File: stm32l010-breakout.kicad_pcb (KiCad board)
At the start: 2 copper layers, 24 x 50 mm, 30 parts, among them J1 SWD, J2 Left, J3 Right, Q1 BC847CDW1, SW1 Reset, U1 STM32L010K8Tx, Y1 32.768kHz

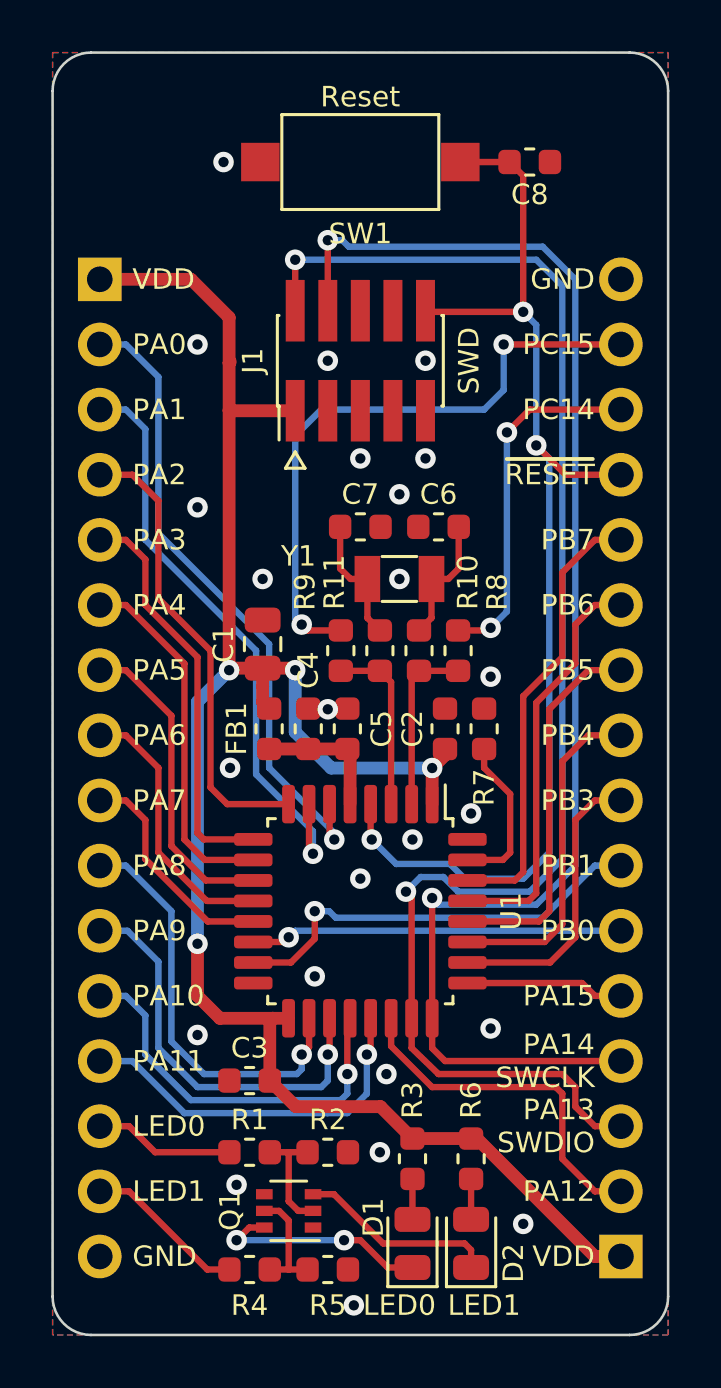
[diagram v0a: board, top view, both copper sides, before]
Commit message: Rotated the SWD connector, moved LED buffer to the front layer
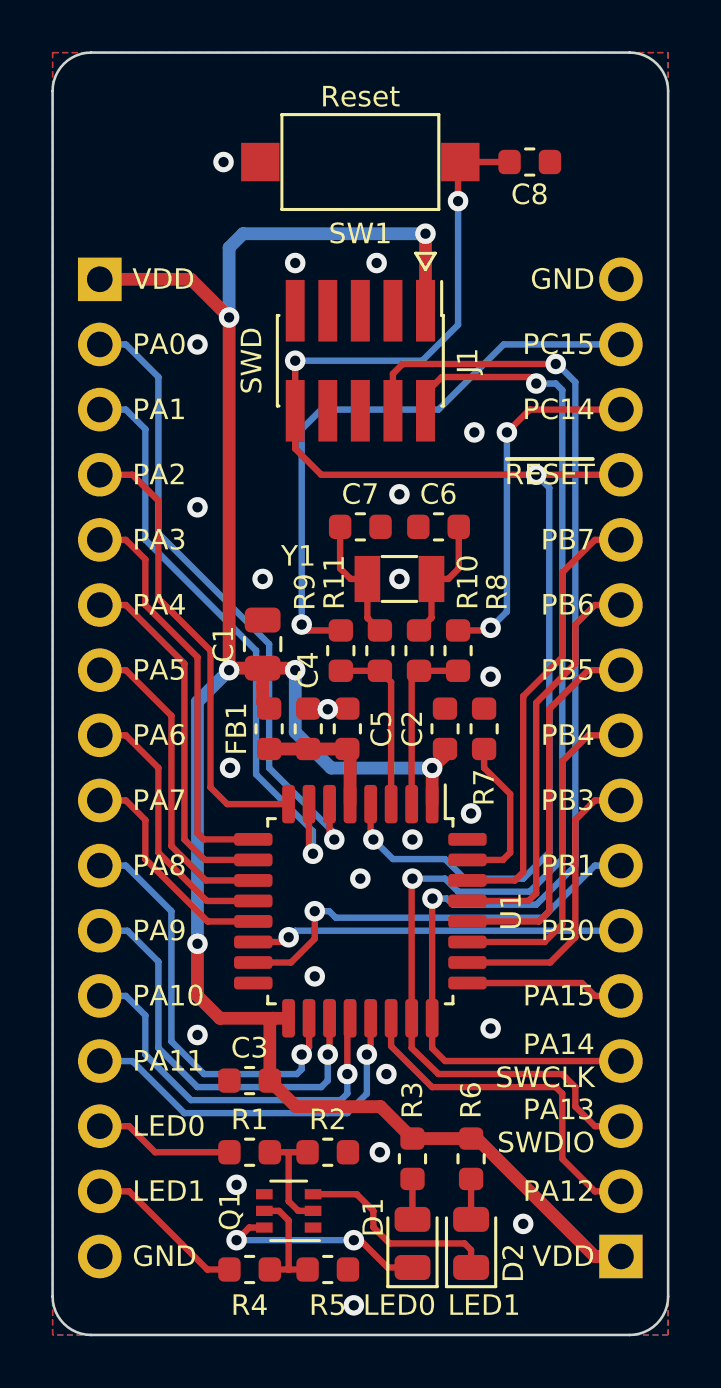
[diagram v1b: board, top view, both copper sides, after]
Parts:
- turned J1 to 270 degrees
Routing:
- net VDD: track 73.2 -> 84.2 mm, vias 4 -> 6
- net /PA13_SWDIO: track 58.3 -> 47.8 mm
- net /~RESET: track 46.5 -> 56.1 mm, vias 3 -> 4
- net /PA14_SWCLK: track 56.1 -> 47.6 mm
- net /PC15: track 24.2 -> 23.1 mm, vias 2 -> 1
- net GND: vias 24 -> 23

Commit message: More PCB tweaks
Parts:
- moved C8 17.2 mm to (124.0, 94.7)
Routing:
- net /~RESET: track 56.1 -> 49.0 mm
- net VDD: track 84.2 -> 85.4 mm
- net GND: vias 23 -> 25

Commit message: Finished (hopefully) layout for the Rev. B
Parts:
- moved #LOGO1 0.38 mm to (135.4, 80.0)
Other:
- board text added: "STM32L010 Breakout Board © 2020 Michal Potrzebicz michal@elevendroids.com CC BY-SA 4.0 Rev. B"
- board text removed: "Rev. B"
- board text removed: "STM32L010 Breakout Board © 2020 Michal Potrzebicz michal@elevendroids.com CC BY-SA 4.0"

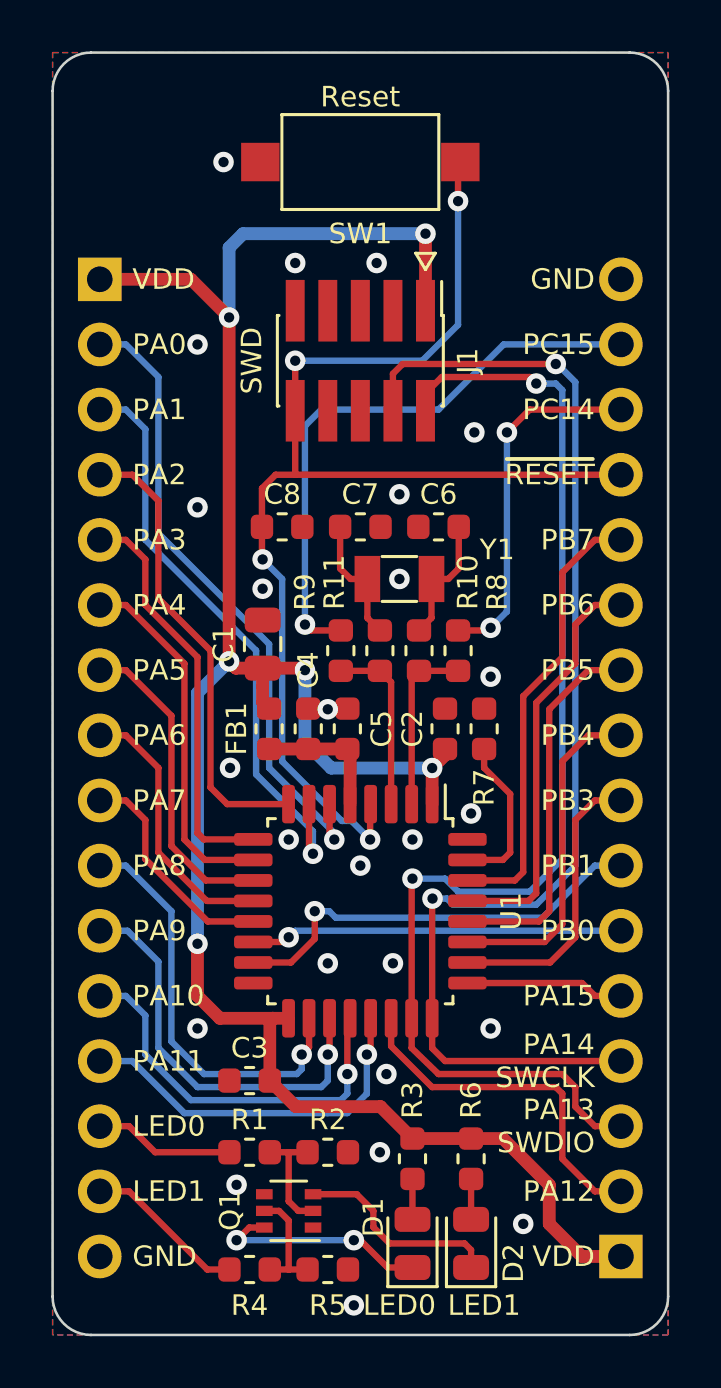
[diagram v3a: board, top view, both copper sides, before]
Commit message: Revision C with a 4 layer PCB, initial commit
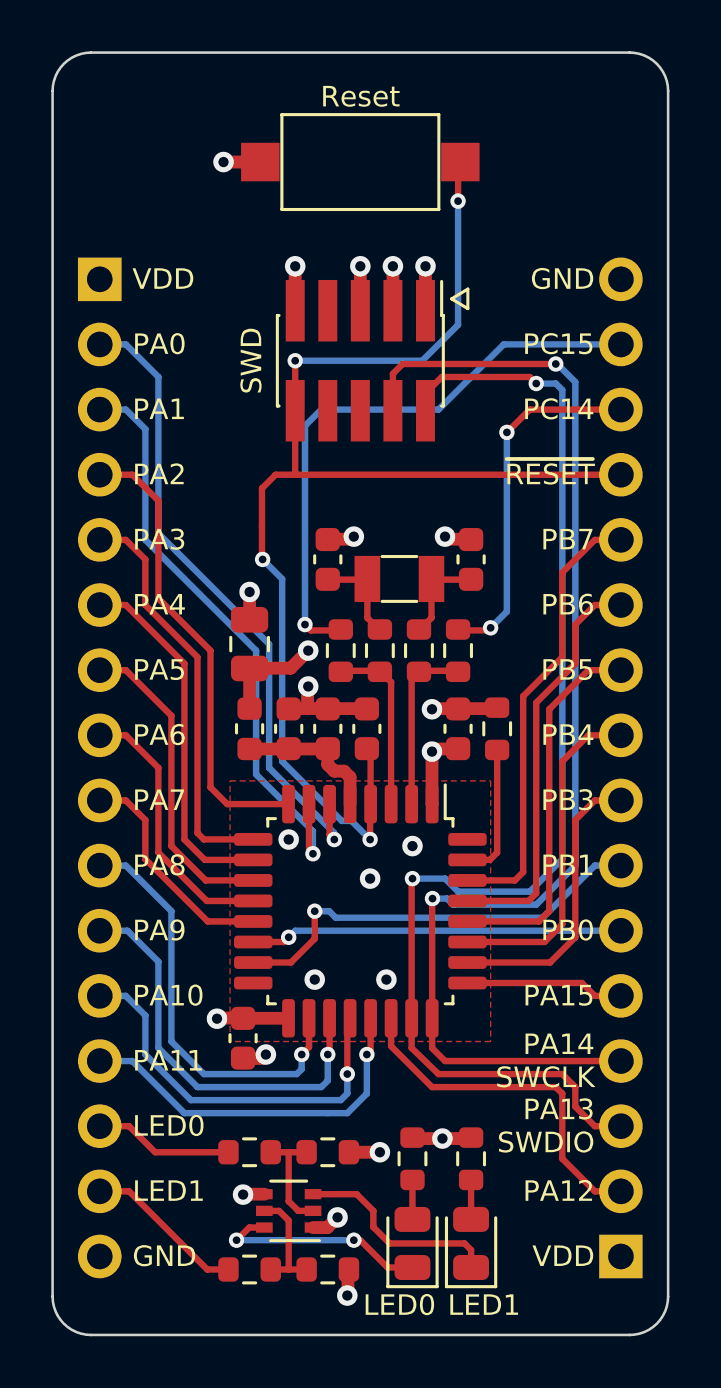
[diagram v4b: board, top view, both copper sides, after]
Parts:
- FB1: value Bead -> 470R/100MHz
- moved C8 8.54 mm to (127.3, 102.6), turned to 90 degrees
- moved C6 1.80 mm to (131.3, 96.0), turned to 90 degrees
- moved C7 1.80 mm to (125.7, 96.0), turned to 90 degrees
- moved C3 1.67 mm to (122.4, 114.7), turned to -90 degrees
- moved C4 0.76 mm to (124.2, 102.6)
- moved C5 0.76 mm to (125.7, 102.6)
- moved FB1 0.76 mm to (122.7, 102.6)
- moved C2 0.51 mm to (130.8, 102.6)
- moved R7 0.51 mm to (132.3, 102.6)
- moved C1 0.51 mm to (122.7, 99.3)
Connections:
- net /~RESET renamed /~{RESET}
- J1 pad 6: Net-(J1-Pad6) -> unconnected-(J1-Pad6)
- J1 pad 7: Net-(J1-Pad7) -> unconnected-(J1-Pad7)
- J1 pad 8: Net-(J1-Pad8) -> unconnected-(J1-Pad8)
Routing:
- net VDD: track 85.4 -> 14.1 mm, vias 6 -> 5
- net GND: track 0.00 -> 21.5 mm, vias 25 -> 19
- net /~{RESET}: track 49.0 -> 51.2 mm
- net Net-(C7-Pad1): track 5.06 -> 3.76 mm
- net Net-(C6-Pad1): track 5.06 -> 3.76 mm
- net Net-(R7-Pad1): track 6.24 -> 5.32 mm
- net VDDA: track 5.24 -> 5.78 mm
- added copper zone on In1.Cu, net GND
- added copper zone on In2.Cu, net VDD
- removed copper zone on B.Cu, net GND
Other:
- copper layers 2 -> 4
- net class Default removed
- net class Power removed
- board text added: "STM32L010 Breakout Board © 2022 Michal Potrzebicz michal@elevendroids.com CC BY-SA 4.0 Rev. C"
- board text added: "~{RESET}"
- board text removed: "STM32L010 Breakout Board © 2020 Michal Potrzebicz michal@elevendroids.com CC BY-SA 4.0 Rev. B"
- board text removed: "~RESET"
